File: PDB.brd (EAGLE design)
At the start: 143.5 x 151.3 mm, 74 parts, among them IC1 LM555N

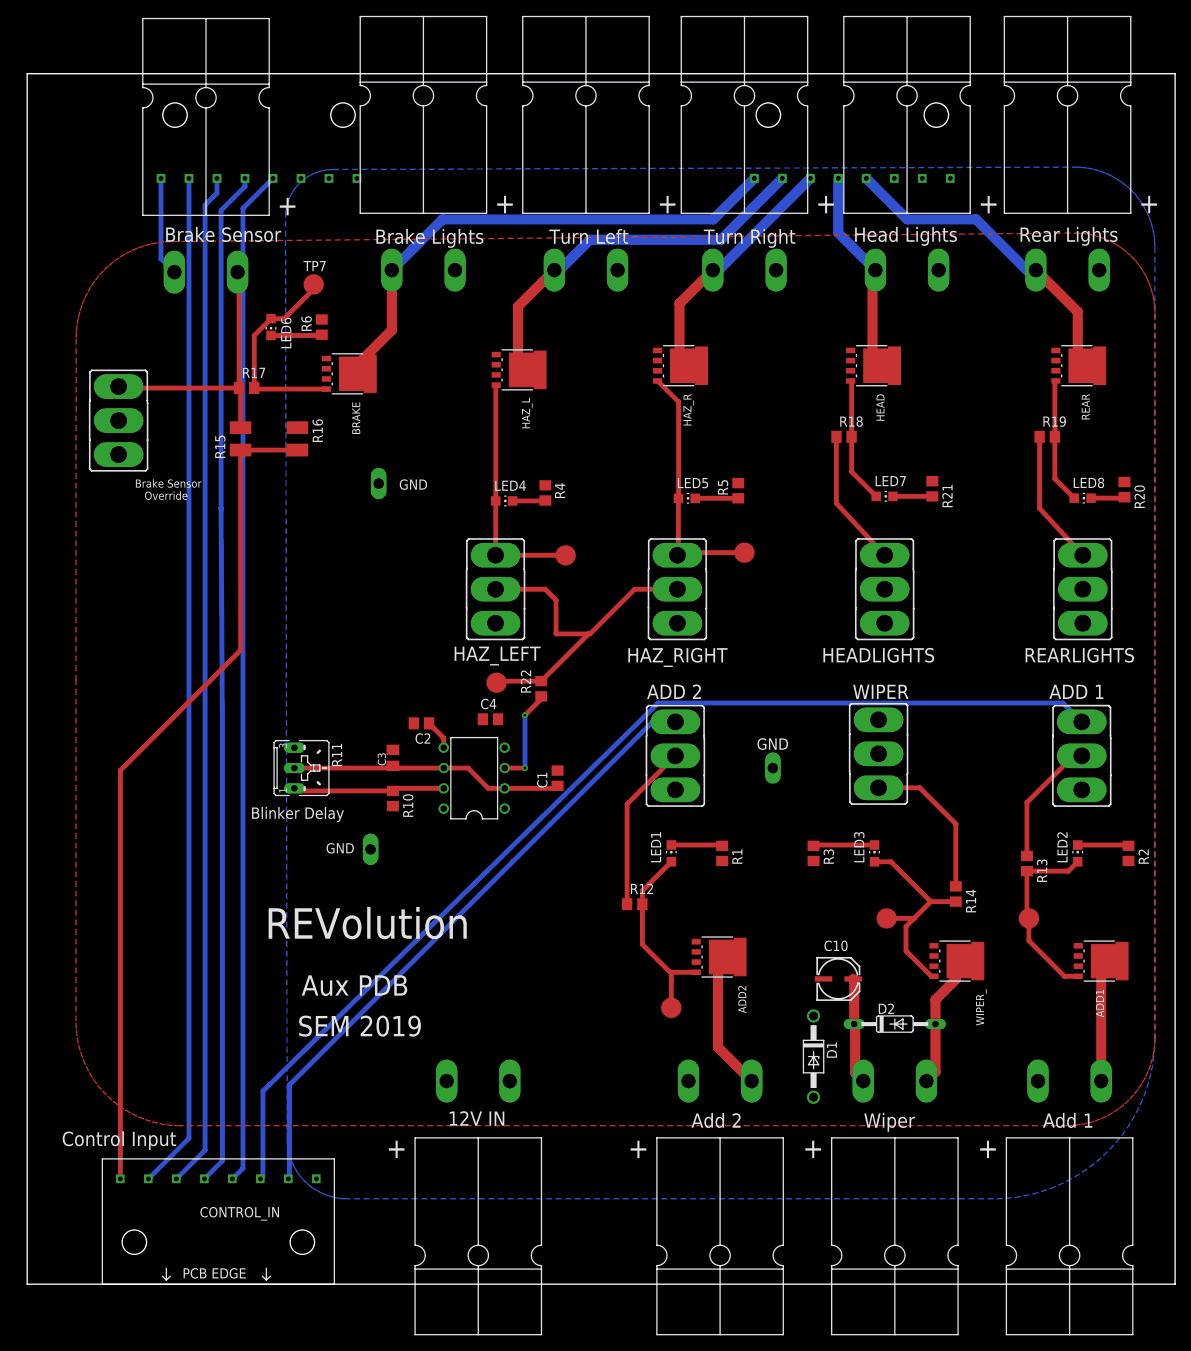
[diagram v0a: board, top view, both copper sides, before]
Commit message: adds clock select jumper
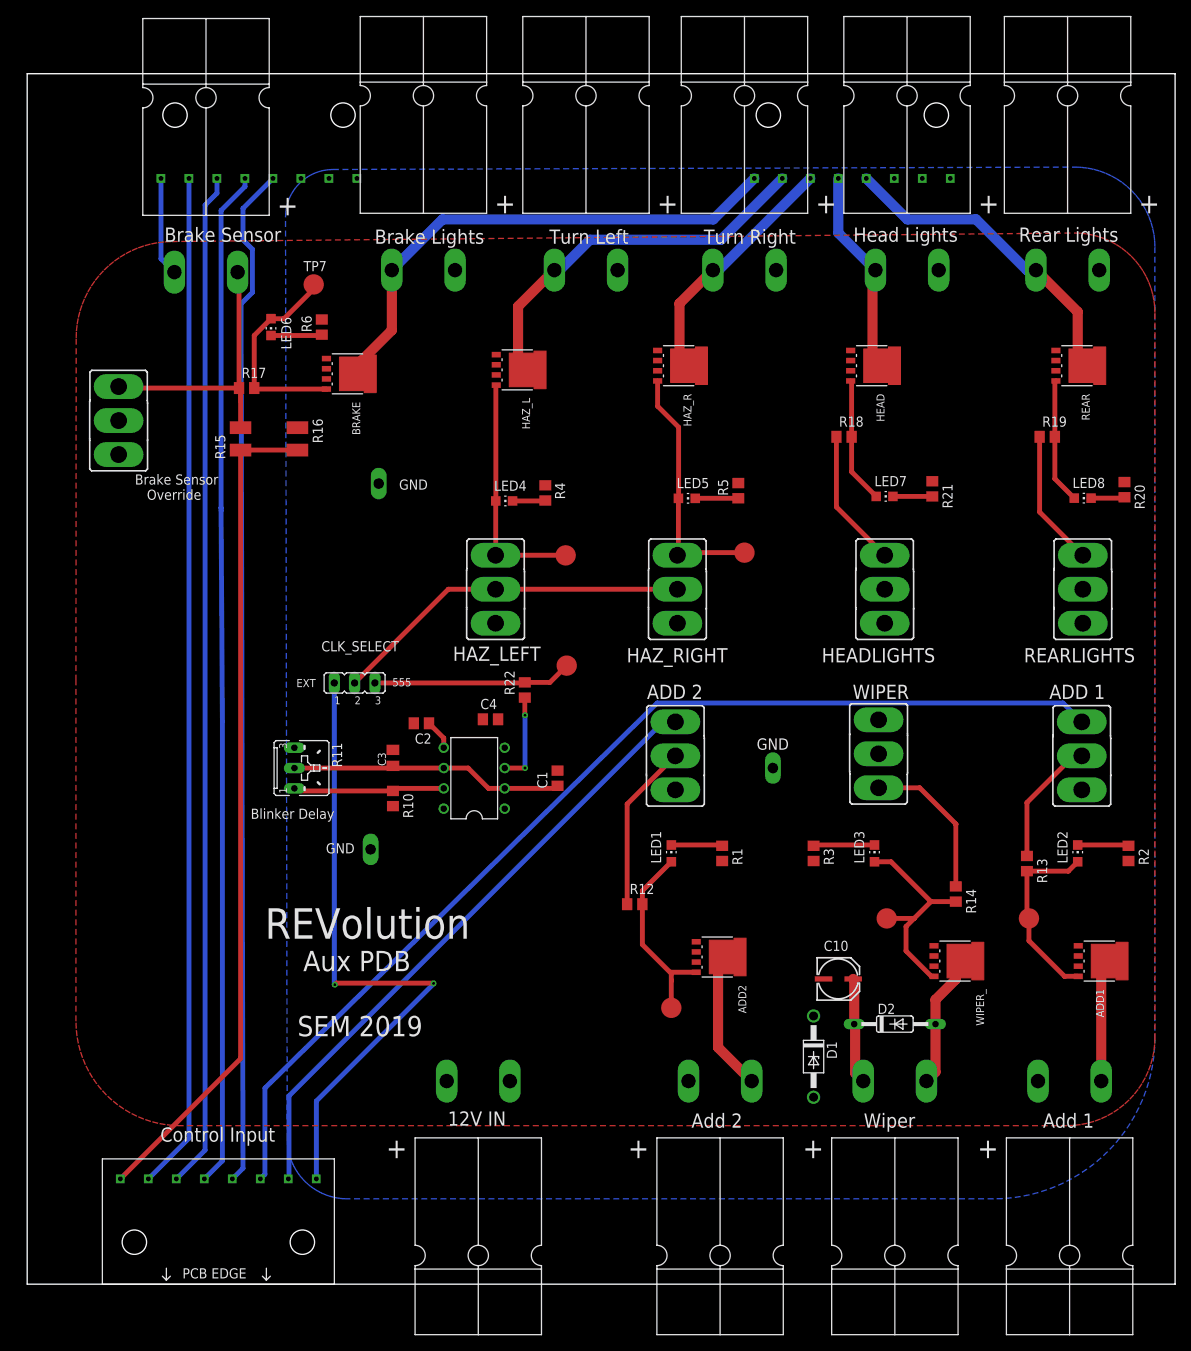
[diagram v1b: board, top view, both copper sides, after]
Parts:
- added CLK_SELECT: (no value), jumper:JP2
- CONTROL_IN: value 8-PIN-MOLEX-RA-FEMALE -> (none)
- moved TP1 9.02 mm to (75.8, 54.0)
- moved R22 2.06 mm to (70.6, 50.9)
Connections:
- new net CLK: CLK_SELECT.2, HAZ_LEFT.2, HAZ_RIGHT.2
- new net EXT_CLK: CLK_SELECT.1, CONTROL_IN.P8
- net 555_OUT: now also CLK_SELECT.3; no longer HAZ_LEFT.2, HAZ_RIGHT.2
- net GND: no longer CONTROL_IN.P8
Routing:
- net EXT_CLK: track 0.00 -> 80.8 mm, vias 0 -> 2
- net CLK: track 0.00 -> 45.2 mm
- net 555_OUT: track 43.9 -> 24.9 mm
- net SCL_SPI: track 127.3 -> 128.4 mm
- net Q: track 12.3 -> 11.4 mm
- net µC_ADD_2: track 78.7 -> 78.1 mm
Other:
- board text added: "555"
- board text added: "EXT"

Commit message: adds jumper to test brake lights
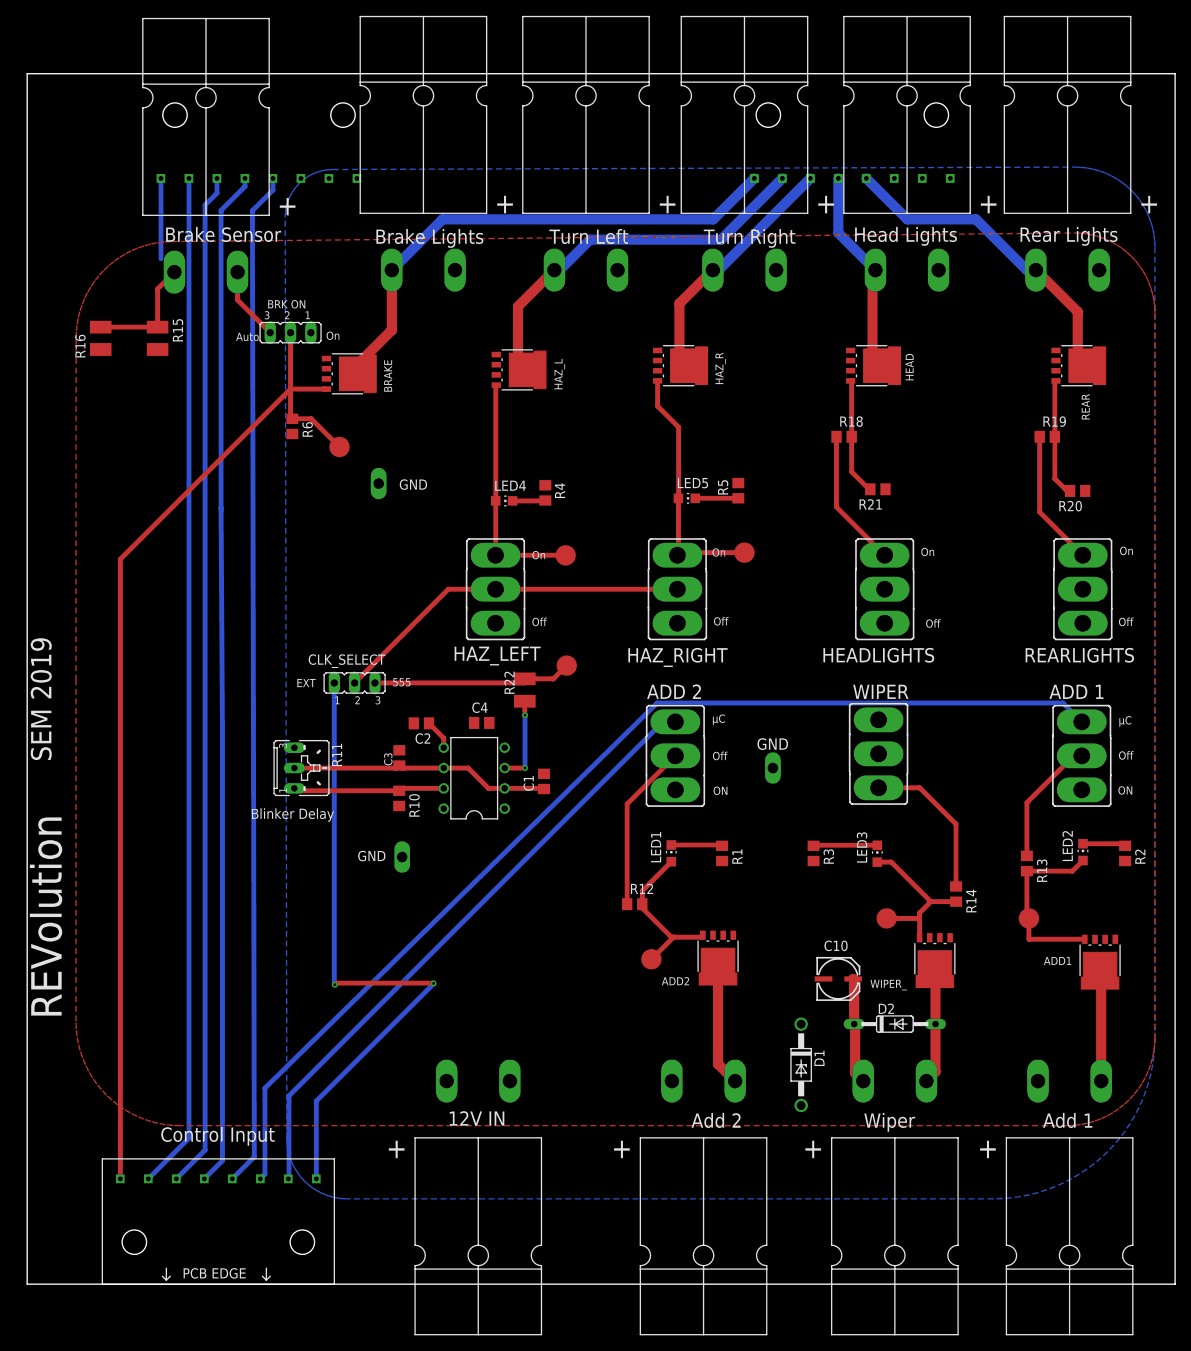
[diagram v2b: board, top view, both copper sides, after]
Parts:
- removed BRAKE_SNS_OVR: (no value), switch:M9040P
- removed LED6, LED7, LED8: (no value), led:CHIP-LED0805
- removed R17: (no value), rcl:R0805
- added BRAKE_SENSOR_OVERRIDE: (no value), jumper:JP2
- C3: device rcl:C0805K -> rcl:C0805
- R1, R2, R20, R21, R3, R6: value 510 -> 1K
- R15: value 12K -> 47K
- R16: value 18K -> 33K
- R22: device rcl:R0805 -> rcl:R3225
- moved R16 27.6 mm to (17.6, 94.9), turned to 90 degrees
- moved TP7 20.6 mm to (47.4, 81.3)
- moved R15 16.3 mm to (24.7, 94.9), turned to 270 degrees
- moved R6 12.9 mm to (41.5, 83.9), turned to 270 degrees
- moved R21 6.80 mm to (114.7, 76.0), turned to 180 degrees
- moved TP2 6.56 mm to (86.4, 17.2)
- moved R20 5.85 mm to (139.7, 75.8), turned to 180 degrees
- moved TP12 4.06 mm to (55.3, 30.0)
- moved WIPER_ 2.63 mm to (121.8, 17.2), turned to 180 degrees
- moved ADD2_OUT 2.07 mm to (92.9, -5.08)
- moved D1 1.86 mm to (105.1, 4.05)
- moved C1 1.74 mm to (73.0, 39.5)
- moved C4 1.18 mm to (65.2, 46.8)
- moved C3 0.80 mm to (54.9, 42.4)
- moved R10 0.78 mm to (54.9, 37.4)
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- renumbered IC1 to 555
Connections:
- removed net BRK_SNS_5V: CONTROL_IN.P1, R15.1, R16.2
- removed net N$10: LED7.C, R21.2
- removed net N$13: BRAKE.4, LED6.A, R17.2, TP7.TP
- removed net N$33: LED6.C, R6.1
- removed net N$9: LED8.C, R20.2
- new net SNS_VOLTAGE: R15.1, R16.2, VDD_IN1.BLACK
- net BRAKE_SNS_IN: now also BRAKE.4, BRAKE_SENSOR_OVERRIDE.2, BRAKE_SENSOR_OVERRIDE.3, CONTROL_IN.P1, R6.1, TP7.TP; no longer BRAKE_SNS_OVR.1, R15.2, R17.1
- net N$14: now also R21.2; no longer LED7.A
- net N$15: now also R20.2; no longer LED8.A
- net VDD: now also BRAKE_SENSOR_OVERRIDE.1, R15.2; no longer BRAKE_SNS_OVR.2, VDD_IN1.BLACK
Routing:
- net BRAKE_SNS_IN: track 34.8 -> 139.5 mm
- net BRK_SNS_5V: track 104.4 -> 0.00 mm
- net N$13: track 26.3 -> 0.00 mm
- net SNS_VOLTAGE: track 0.00 -> 14.9 mm
- net N$22: track 28.0 -> 21.3 mm
- net N$33: track 6.39 -> 0.00 mm
- net N$10: track 4.92 -> 0.00 mm
- net N$9: track 4.36 -> 0.00 mm
- net N$7: track 24.5 -> 21.1 mm
- net VDD: track 25.8 -> 23.4 mm
- net TR/THR: track 34.3 -> 32.6 mm
- net N$14: track 15.7 -> 14.6 mm
- net N$28: track 6.39 -> 5.37 mm
- net SCL_SPI: track 128.4 -> 127.4 mm
- net N$15: track 15.7 -> 14.8 mm
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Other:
- board text added: "Auto"
- board text added: "BRK ON"
- board text added: "ON"
- board text added: "Off"
- board text added: "On"
- board text added: "µC"
- board text removed: "Aux PDB"
- board text removed: "Brake Sensor Override"

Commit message: redoes ground plane, fixes names of components by centering
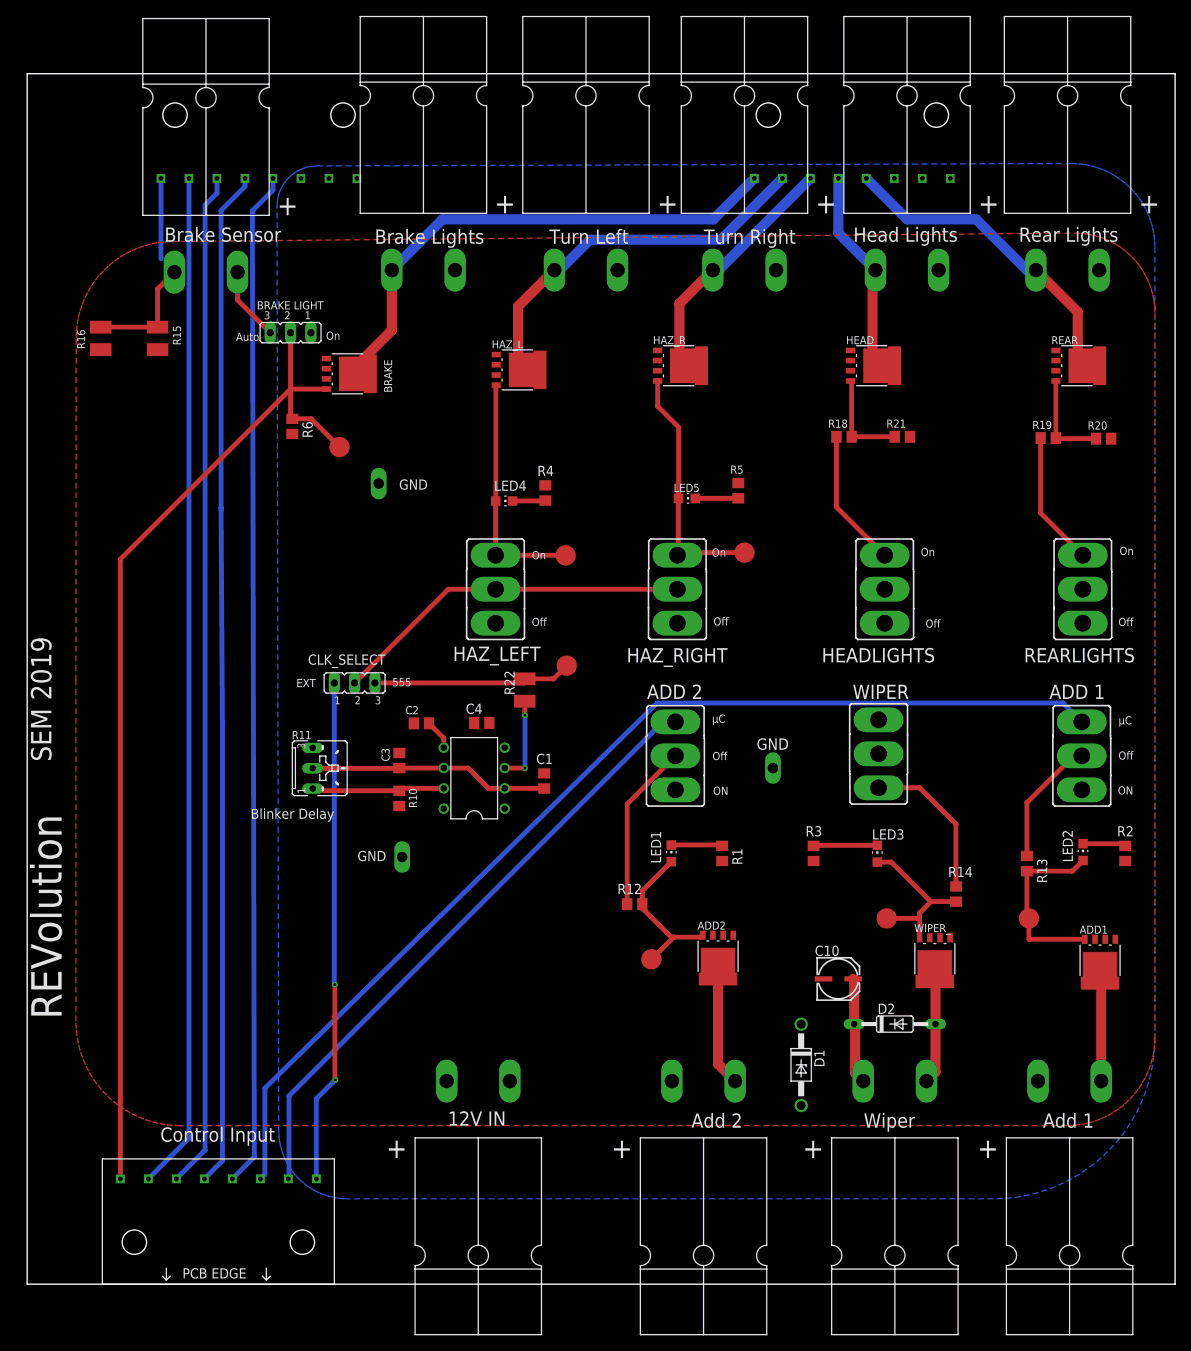
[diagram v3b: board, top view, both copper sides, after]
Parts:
- moved R20 7.29 mm to (142.9, 82.3)
- moved R21 7.24 mm to (117.8, 82.6)
- moved R11 2.29 mm to (45.0, 41.1)
- moved C3 0.34 mm to (54.9, 42.1)
- moved R19 0.20 mm to (136.0, 82.4)
- moved C1 0.07 mm to (73.0, 39.5)
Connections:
- net GND: no longer R11.E
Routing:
- net EXT_CLK: track 80.8 -> 63.1 mm
- net N$15: track 14.8 -> 12.2 mm
- net TR/THR: track 32.6 -> 30.0 mm
- net DIS: track 18.9 -> 16.6 mm
- net N$14: track 14.6 -> 12.4 mm
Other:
- board text added: "BRAKE LIGHT"
- board text removed: "BRK ON"

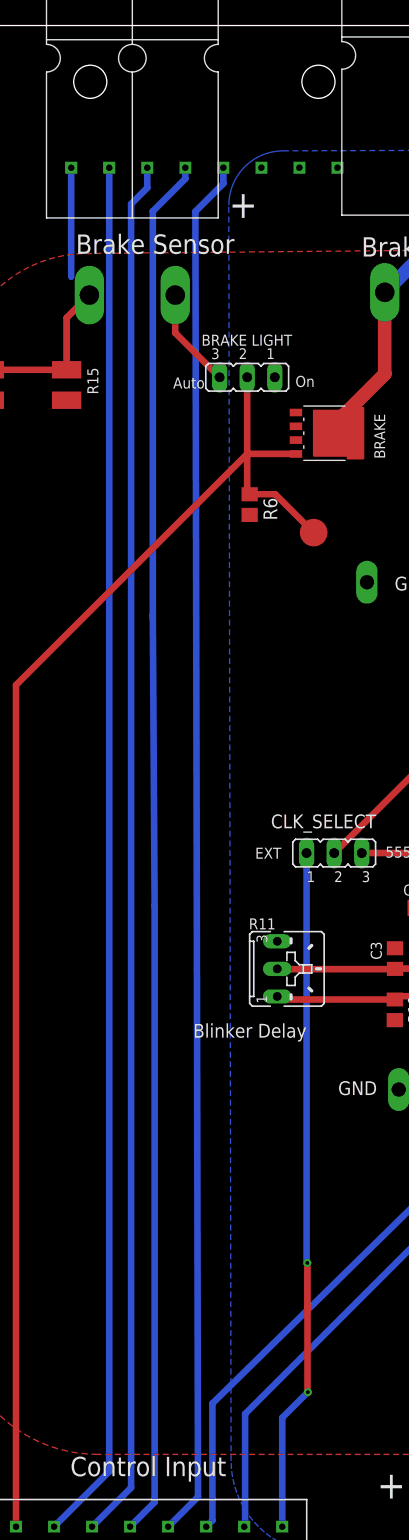
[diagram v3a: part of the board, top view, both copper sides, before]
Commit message: messed around with BitMaP, changes orientation of Molex conn on bottom
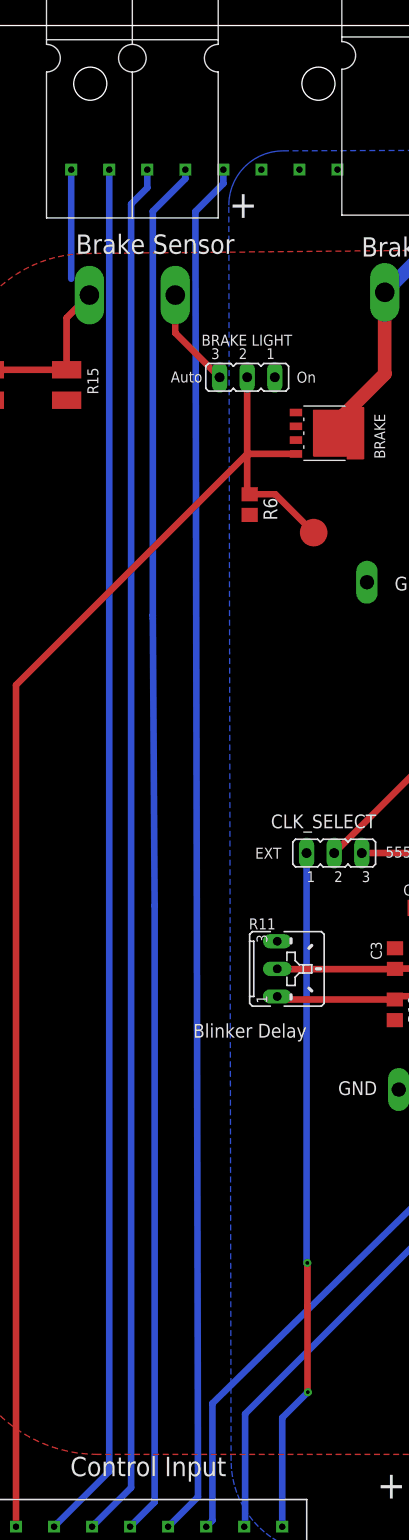
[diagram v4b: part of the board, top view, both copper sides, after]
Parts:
- moved SPI_OUT 0.18 mm to (22.9, 127.8)
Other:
- board text added: "INDICATOR OUT"
